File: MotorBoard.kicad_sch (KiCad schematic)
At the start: 42 parts, among them J1 Screw_Terminal_01x04, J2 Screw_Terminal_01x04, J3 Screw_Terminal_01x04, J4 Screw_Terminal_01x02, J5 USB_B_Micro, Q1 Q_NPN_BEC, Q2 Q_NPN_BEC, SW1 SW_SPST, SW2 SW_SPST, U1 MC34063AD, U2 ESP32-WROVER-E, U3 MC34063AD, U4 CH340C

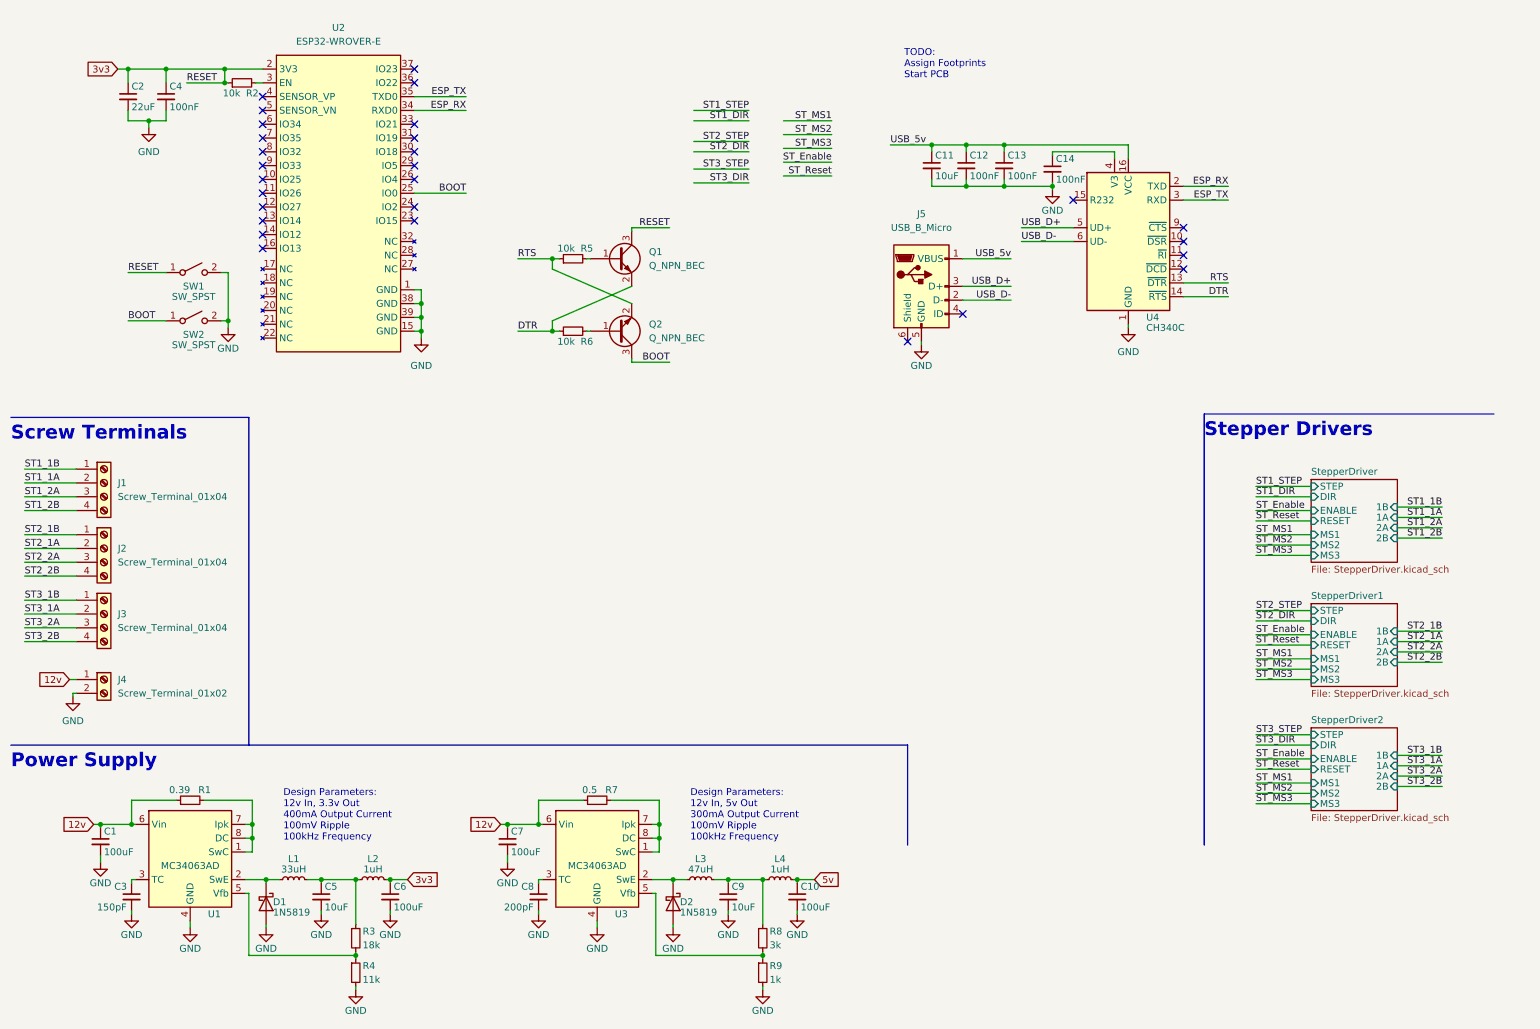
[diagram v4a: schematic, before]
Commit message: Added servo headers
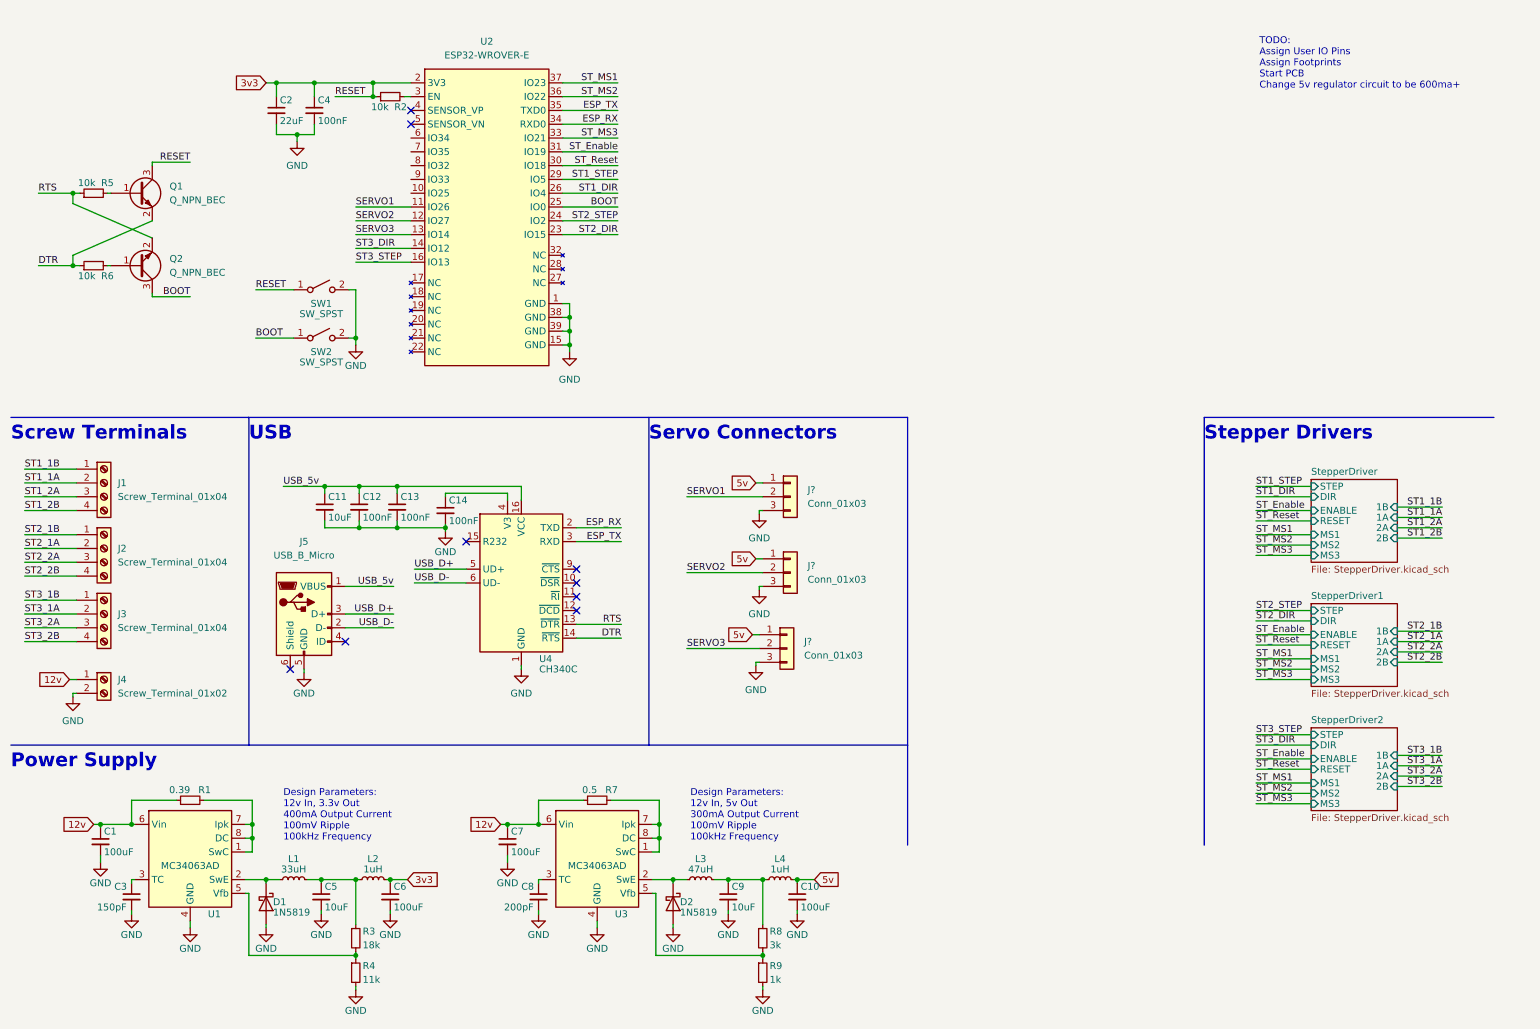
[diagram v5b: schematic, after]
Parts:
- added J? (x3): Conn_01x03, Connector_PinHeader_2.54mm:PinHeader_1x03_P2.54mm_Vertical, symbol Connector_Generic:Conn_01x03
- R1: LSCS Part Number (none) -> C469654; Manufacturer Part Number (none) -> RL0603FR-070R39L
- R3: LSCS Part Number (none) -> C25810; Manufacturer Part Number (none) -> 0603WAF1802T5E
- R4: LSCS Part Number (none) -> C103227; Manufacturer Part Number (none) -> RTT031102FTP
- R7: LSCS Part Number (none) -> C247569; Manufacturer Part Number (none) -> 0603WAJ050KT5E
- R8: LSCS Part Number (none) -> C126358; Manufacturer Part Number (none) -> RC0603FR-073KL
- R9: LSCS Part Number (none) -> C22548; Manufacturer Part Number (none) -> RC0603FR-071KL
- SW1, SW2: footprint (none) -> MotorBoard:TS-1101-C-W
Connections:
- net 5v: now also J?.1 (Pin_1), J?.1 (Pin_1), J?.1 (Pin_1)
- net GND: now also J?.3 (Pin_3), J?.3 (Pin_3), J?.3 (Pin_3)
- net ST1_DIR: now also U2.26 (IO4)
- net ST1_STEP: now also U2.29 (IO5)
- net ST2_DIR: now also U2.23 (IO15)
- net ST2_STEP: now also U2.24 (IO2)
- net ST3_DIR: now also U2.14 (IO12)
- net ST3_STEP: now also U2.16 (IO13)
- net ST_Enable: now also U2.31 (IO19)
- net ST_MS1: now also U2.37 (IO23)
- net ST_MS2: now also U2.36 (IO22)
- net ST_MS3: now also U2.33 (IO21)
- net ST_Reset: now also U2.30 (IO18)
- net SERVO1: now reaches U2.11 (IO26)
- net SERVO1: now also J?.2 (Pin_2)
- net SERVO2: now reaches U2.12 (IO27)
- net SERVO2: now also J?.2 (Pin_2)
- net SERVO3: now reaches U2.13 (IO14)
- net SERVO3: now also J?.2 (Pin_2)
- no-connect marks 28 -> 9
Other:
- note added: "Servo Connectors"
- note added: "TODO: Assign User IO Pins Assign Footprints Start PCB Change 5v regulator circuit to be 600ma+"
- note added: "USB"
- note removed: "TODO: Assign Footprints Start PCB"
- moved on the sheet: C11, C12, C13, C14, C2, C4, J5, Q1, Q2, R2, R5, R6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

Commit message: Began work on PCB layout
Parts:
- gave numbers to parts that had none: 3
- renumbered C14 to C10, C7 to C11, C8 to C12, C9 to C13, C10 to C14, C3 to C2, C2 to C3, C11 to C6, C12 to C7, C6 to C8, C13 to C9, R5 to R1, R6 to R2, R1 to R3, R3 to R4, R4 to R5, R2 to R6, U4 to U3, U3 to U4
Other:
- note added: "ESP32"
